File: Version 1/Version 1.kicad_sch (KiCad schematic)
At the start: 1 part, among them U1 YAAJ_BlackPill_SWD_Breakout

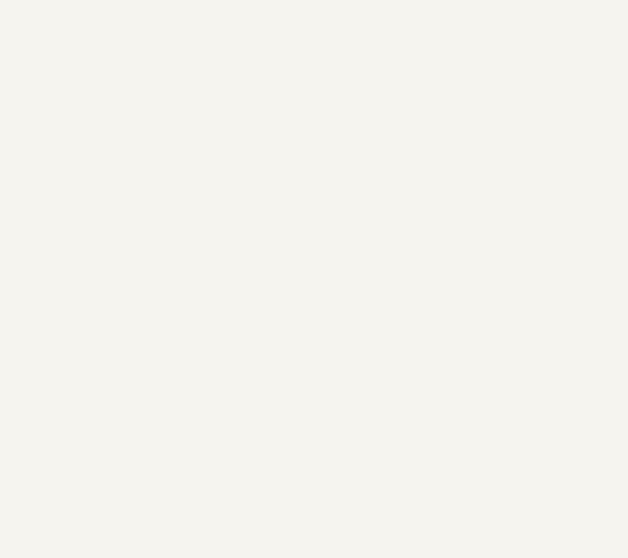
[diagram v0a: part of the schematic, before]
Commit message: added hal sensor data
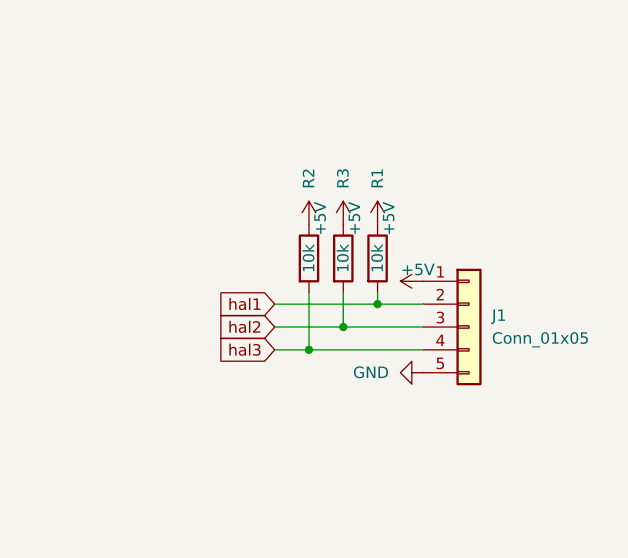
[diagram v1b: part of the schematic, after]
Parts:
- added J1: Conn_01x05, symbol Connector_Generic:Conn_01x05
- added R1, R2, R3: 10k, symbol Device:R
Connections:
- new net +5V: J1.1 (Pin_1), R1.1, R2.1, R3.1
- new net GND: J1.5 (Pin_5)
- new net hal1: J1.2 (Pin_2), R1.2
- new net hal2: J1.3 (Pin_3), R3.2
- new net hal3: J1.4 (Pin_4), R2.2

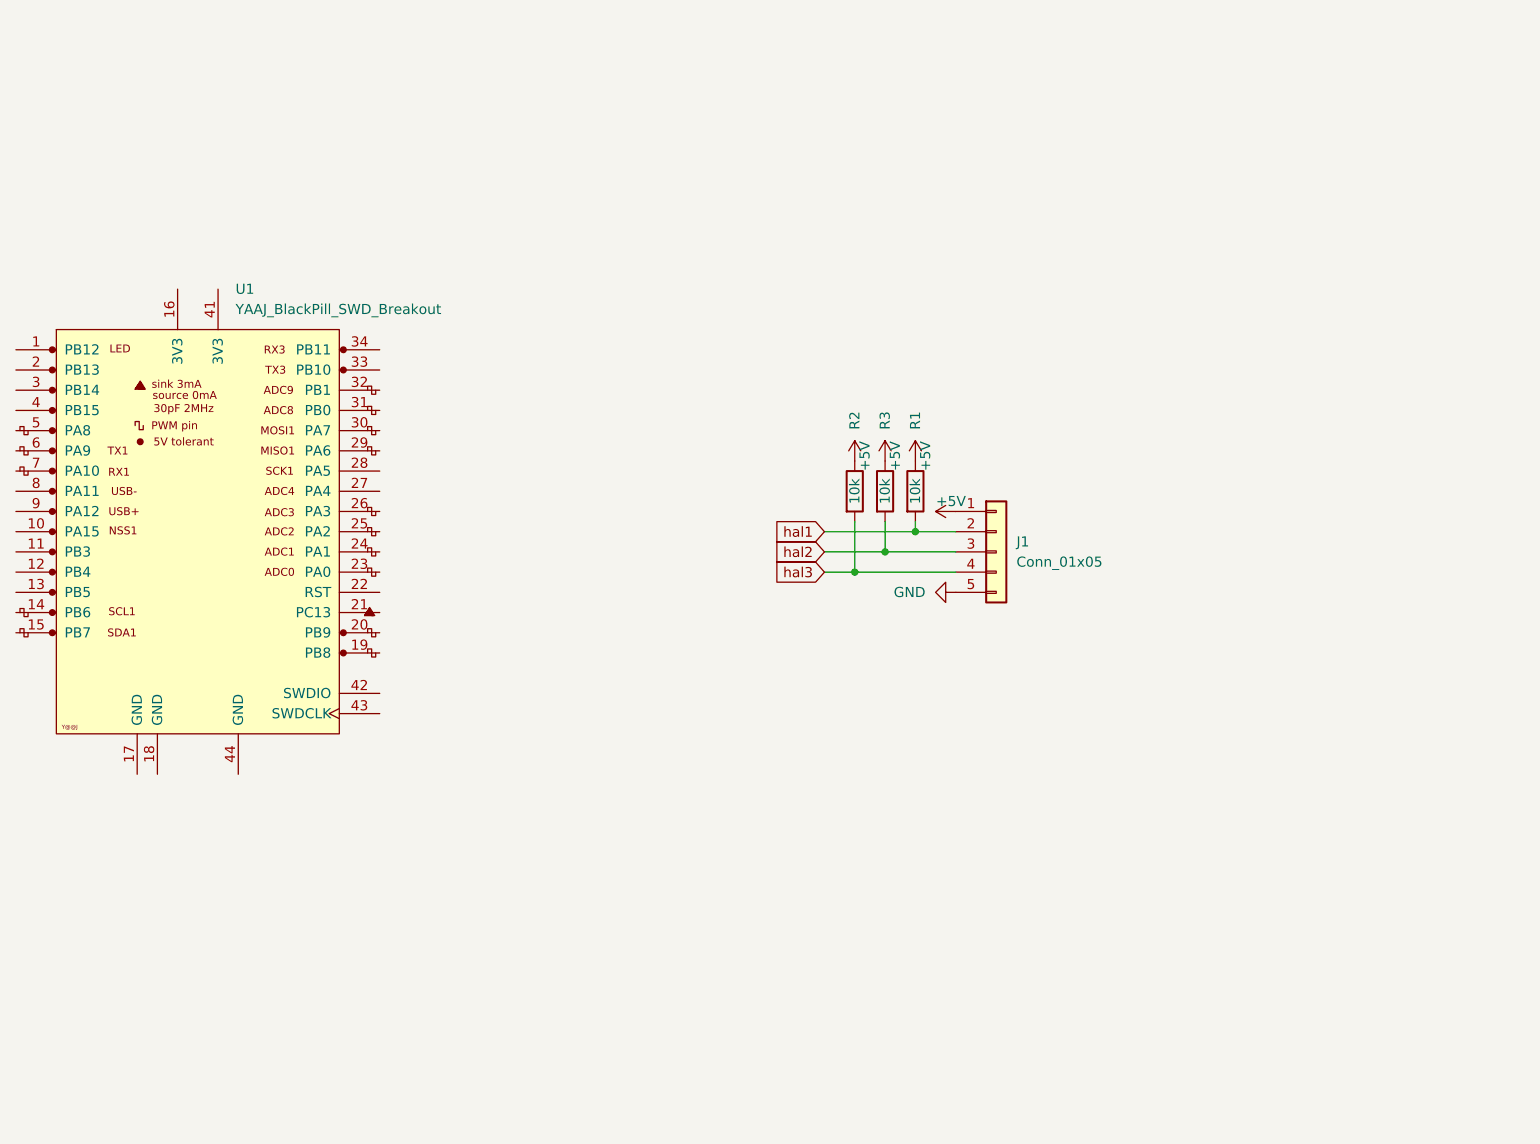
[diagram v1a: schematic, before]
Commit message: added extra regulators
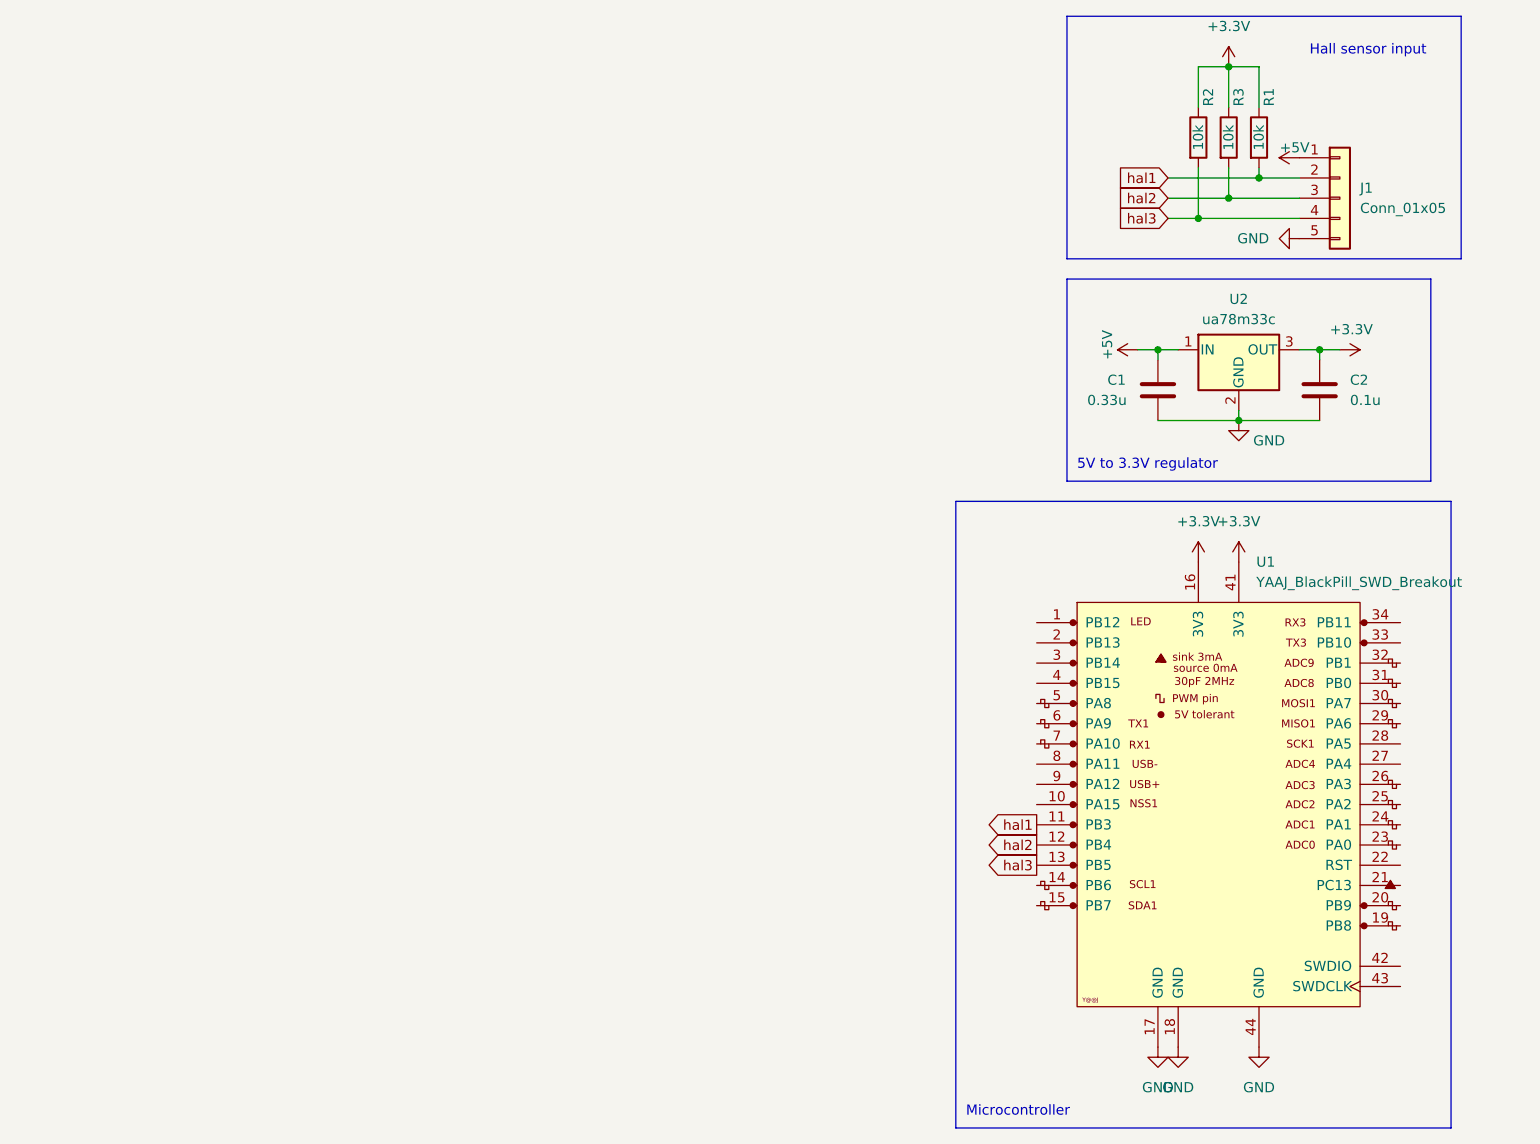
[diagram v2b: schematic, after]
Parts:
- added C1: 0.33u, symbol Device:C
- added C2: 0.1u, symbol Device:C
- added U2: ua78m33c, symbol Regulator_Linear:ua78m33c
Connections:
- net +5V: now also C1.1, U2.1 (IN); no longer R1.1, R2.1, R3.1
- net GND: now also U1.17 (GND), U1.18 (GND), U1.44 (GND), C1.2, C2.2, U2.2 (GND)
- net hal1: now also U1.11 (PB3)
- net hal2: now also U1.12 (PB4)
- net hal3: now also U1.13 (PB5)
- net +3.3V: now reaches U1.16 (3V3)
- net +3.3V: now also R1.1, R2.1, R3.1, U1.41 (3V3), C2.1, U2.3 (OUT)
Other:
- note added: "5V to 3.3V regulator"
- note added: "Hall sensor input"
- note added: "Microcontroller"
- moved on the sheet: J1, R1, R2, R3, U1

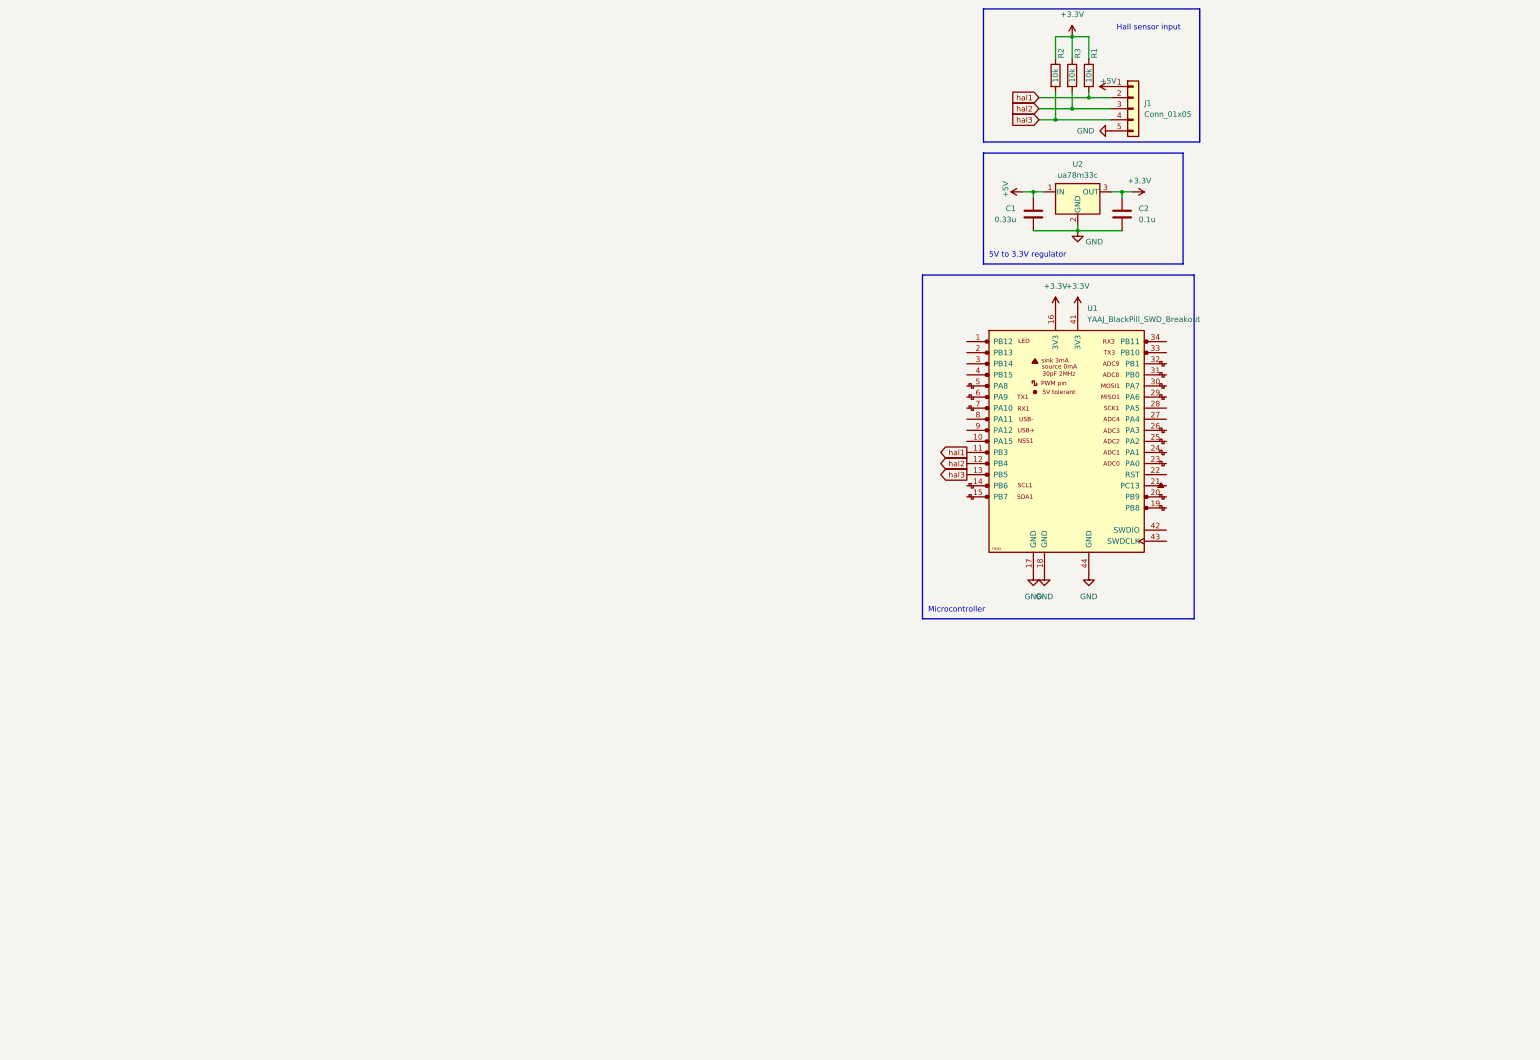
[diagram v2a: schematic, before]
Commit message: updated some schem files
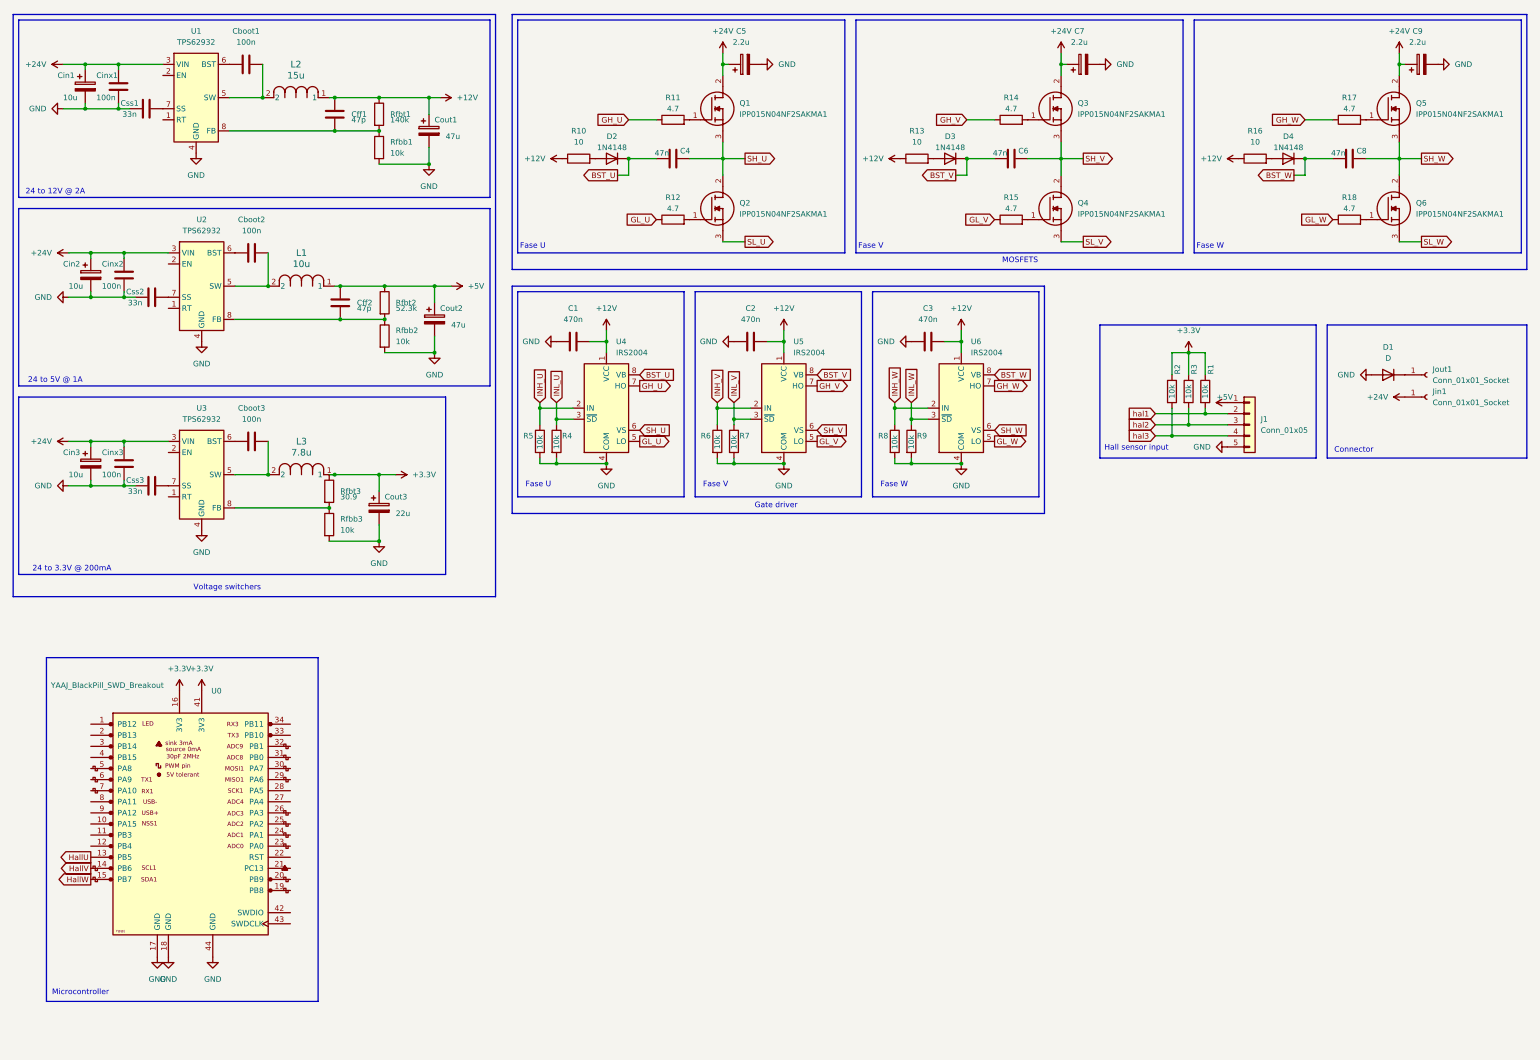
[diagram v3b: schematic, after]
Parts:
- removed U2: ua78m33c, symbol Regulator_Linear:ua78m33c
- added C3: 470n, symbol Device:C
- added C4, C6, C8: 47n, symbol Device:C
- added C5, C7, C9: 2.2u, symbol Device:C_Polarized
- added Cboot1, Cboot2, Cboot3, Cinx1, Cinx2, Cinx3: 100n, Capacitor_THT:C_Disc_D3.4mm_W2.1mm_P2.50mm, symbol Device:C
- added Cff1, Cff2: 47p, Capacitor_THT:C_Disc_D3.4mm_W2.1mm_P2.50mm, symbol Device:C
- added Cin1, Cin2, Cin3: 10u, Capacitor_THT:CP_Radial_D5.0mm_P2.50mm, symbol Device:C_Polarized
- added Cout1, Cout2: 47u, Capacitor_THT:CP_Radial_D12.5mm_P5.00mm, symbol Device:C_Polarized
- added Cout3: 22u, Capacitor_THT:CP_Radial_D12.5mm_P5.00mm, symbol Device:C_Polarized
- added Css1, Css2, Css3: 33n, Capacitor_THT:C_Disc_D3.4mm_W2.1mm_P2.50mm, symbol Device:C
- added D1: D, Diode_THT:D_DO-34_SOD68_P12.70mm_Horizontal, symbol Device:D
- added D2, D3, D4: 1N4148, Diode_THT:D_DO-35_SOD27_P7.62mm_Horizontal, symbol Diode:1N4148
- added Jin1, Jout1: Conn_01x01_Socket, MountingHole:MountingHole_4.3mm_M4_DIN965_Pad, symbol Connector:Conn_01x01_Socket
- added L1: 10u, IND_MULTICOMP_MCSCH895_MTC, symbol 2024-02-15_20-52-33:MCSCH895-100LU
- added L2: 15u, IND_MULTICOMP_MCSCH895_MTC, symbol 2024-02-15_20-52-33:MCSCH895-100LU
- added L3: 7.8u, IND_MULTICOMP_MCSCH895_MTC, symbol 2024-02-15_20-52-33:MCSCH895-100LU
- added Q1, Q2, Q3, Q4, Q5, Q6: IPP015N04NF2SAKMA1, TO254P475X1028X1996-3P, symbol IPP015N04NF2SAKMA1:IPP015N04NF2SAKMA1
- added R10, R13, R16: 10, symbol Device:R
- added R11, R12, R14, R15, R17, R18: 4.7, symbol Device:R
- added R4, R5, R6, R7, R8, R9: 10k, symbol Device:R
- added Rfbb1, Rfbb2, Rfbb3: 10k, Resistor_THT:R_Axial_DIN0207_L6.3mm_D2.5mm_P10.16mm_Horizontal, symbol Device:R
- added Rfbt1: 140k, Resistor_THT:R_Axial_DIN0207_L6.3mm_D2.5mm_P10.16mm_Horizontal, symbol Device:R
- added Rfbt2: 52.3k, Resistor_THT:R_Axial_DIN0207_L6.3mm_D2.5mm_P10.16mm_Horizontal, symbol Device:R
- added Rfbt3: 30.9, Resistor_THT:R_Axial_DIN0207_L6.3mm_D2.5mm_P10.16mm_Horizontal, symbol Device:R
- added U1, U2, U3: TPS62932, Package_TO_SOT_SMD:SOT-583-8, symbol Regulator_Switching:TPS62932
- added U4, U5, U6: IRS2004, symbol Driver_FET:IRS2004
- C1: value 0.33u -> 470n
- C2: value 0.1u -> 470n
- J1: footprint (none) -> Connector_PinHeader_1.27mm:PinHeader_1x05_P1.27mm_Vertical
- R1, R2, R3: footprint (none) -> Resistor_THT:R_Axial_DIN0207_L6.3mm_D2.5mm_P10.16mm_Horizontal
- renumbered U1 to U0
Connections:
- net +3.3V: now also Cout3.1, L3.1, Rfbt3.1; no longer C2.1
- net +5V: now also Cff2.1, Cout2.1, L1.1, Rfbt2.1; no longer C1.1
- net GND: now also C1.1, C2.1, C3.1, C5.2, C7.2, C9.2, Cin1.2, Cin2.2, Cin3.2, Cinx1.2, Cinx2.2, Cinx3.2, Cout1.2, Cout2.2, Cout3.2, Css1.1, Css2.1, Css3.1, D1.2 (A), R4.2, R5.2, R6.2, R7.2, R8.2, R9.2, Rfbb1.2, Rfbb2.2, Rfbb3.2, U1.4 (GND), U2.4 (GND), U3.4 (GND), U4.4 (COM), U5.4 (COM), U6.4 (COM); no longer C1.2, C2.2
- net hal1: no longer U0.11 (PB3)
- net hal2: no longer U0.12 (PB4)
- net hal3: no longer U0.13 (PB5)
- net HallV: now reaches U0.14 (PB6)
- net HallW: now reaches U0.15 (PB7)
- new net: Cboot2.2, L1.2, U2.5 (SW)
- new net: Q6.1, R18.2
- new net: Q2.1, R12.2
- new net: D4.2 (A), R16.2
- new net: D1.1 (K), Jout1.1 (Pin_1)
- new net: Cff1.2, Rfbb1.1, Rfbt1.2, U1.8 (FB)
- new net: Css3.2, U3.7 (SS)
- new net: D3.2 (A), R13.2
- new net: D2.2 (A), R10.2
- new net: Q3.1, R14.2
- new net: Cboot1.1, U1.6 (BST)
- new net: Cboot1.2, L2.2, U1.5 (SW)
- new net: Cboot2.1, U2.6 (BST)
- new net: Css2.2, U2.7 (SS)
- new net: Cff2.2, Rfbb2.1, Rfbt2.2, U2.8 (FB)
- new net: Css1.2, U1.7 (SS)
- new net: Q5.1, R17.2
- new net: Cboot3.2, L3.2, U3.5 (SW)
- new net: Q1.1, R11.2
- new net: Cboot3.1, U3.6 (BST)
- new net: Rfbb3.1, Rfbt3.2, U3.8 (FB)
- new net: Q4.1, R15.2
- new net +12V: C1.2, C2.2, C3.2, Cff1.1, Cout1.1, L2.1, R10.1, R13.1, R16.1, Rfbt1.1, U4.1 (VCC), U5.1 (VCC), U6.1 (VCC)
- new net +24V: C5.1, C7.1, C9.1, Cin1.1, Cin2.1, Cin3.1, Cinx1.1, Cinx2.1, Cinx3.1, Jin1.1 (Pin_1), Q1.2, Q3.2, Q5.2, U1.3 (VIN), U2.3 (VIN), U3.3 (VIN)
- new net BST_U: C4.1, D2.1 (K), U4.8 (VB)
- new net BST_V: C6.1, D3.1 (K), U5.8 (VB)
- new net BST_W: C8.1, D4.1 (K), U6.8 (VB)
- new net GH_U: R11.1, U4.7 (HO)
- new net GH_V: R14.1, U5.7 (HO)
- new net GH_W: R17.1, U6.7 (HO)
- new net GL_U: R12.1, U4.5 (LO)
- new net GL_V: R15.1, U5.5 (LO)
- new net GL_W: R18.1, U6.5 (LO)
- new net HallU: U0.13 (PB5)
- new net INH_U: R5.1, U4.2 (IN)
- new net INH_V: R6.1, U5.2 (IN)
- new net INH_W: R8.1, U6.2 (IN)
- new net INL_U: R4.1, U4.3 (~{SD})
- new net INL_V: R7.1, U5.3 (~{SD})
- new net INL_W: R9.1, U6.3 (~{SD})
- new net SH_U: C4.2, Q1.3, Q2.2, U4.6 (VS)
- new net SH_V: C6.2, Q3.3, Q4.2, U5.6 (VS)
- new net SH_W: C8.2, Q5.3, Q6.2, U6.6 (VS)
- new net SL_U: Q2.3
- new net SL_V: Q4.3
- new net SL_W: Q6.3
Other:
- note added: "24 to 12V @ 2A"
- note added: "24 to 3.3V @ 200mA"
- note added: "24 to 5V @ 1A"
- note added: "Connector"
- note added: "Fase U"
- note added: "Fase V"
- note added: "Fase W"
- note added: "Gate driver"
- note added: "MOSFETS"
- note added: "Voltage switchers"
- note removed: "5V to 3.3V regulator"
- moved on the sheet: J1, R1, R2, R3, U0

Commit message: updated schem
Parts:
- removed U0: YAAJ_BlackPill_SWD_Breakout, Footprints:YAAJ_BlackPill_SWD_1, symbol YAAJ_BlackPill_SWD_Breakout:YAAJ_BlackPill_SWD_Breakout
- added U7: YAAJ_BlackPill_SWD_BreakoutV2, STM32:Blackpill, symbol YAAJ_BlackPill_SWD_BreakoutV2:YAAJ_BlackPill_SWD_BreakoutV2
- C1, C2, C3, C4, C6, C8: footprint (none) -> Capacitor_THT:C_Disc_D3.4mm_W2.1mm_P2.50mm
- C5, C7, C9: footprint (none) -> Capacitor_THT:CP_Radial_D5.0mm_P2.50mm
- L1, L2, L3: footprint IND_MULTICOMP_MCSCH895_MTC -> Inductor_THT:L_Axial_L13.0mm_D4.5mm_P7.62mm_Vertical_Fastron_HCCC
- Q1, Q2, Q3, Q4, Q5, Q6: footprint TO254P475X1028X1996-3P -> LIB_IPP015N04NF2SAKMA1:TO254P475X1028X1996-3P
- R10, R11, R12, R13, R14, R15, R16, R17, R18, R4, R5, R6, R7, R8, R9: footprint (none) -> Resistor_THT:R_Axial_DIN0207_L6.3mm_D2.5mm_P10.16mm_Horizontal
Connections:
- net +3.3V: now also U7.18 (3V3), U7.40 (3V3), U7.41 (3V3)
- net GND: now also U7.19 (GND), U7.39 (GND), U7.44 (GND)
- net HallU: now also U7.2 (C13)
- net HallV: now also U7.3 (C14)
- net HallW: now also U7.4 (C15)
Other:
- company: (none) -> ALSET
- title: (none) -> Motor driver
